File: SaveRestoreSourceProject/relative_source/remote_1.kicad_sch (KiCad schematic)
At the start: 0 parts

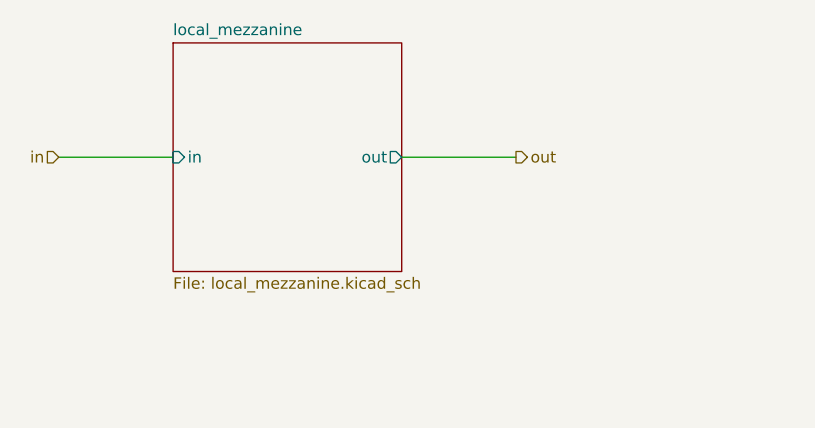
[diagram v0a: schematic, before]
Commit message: Add support for connected drawings, update test template
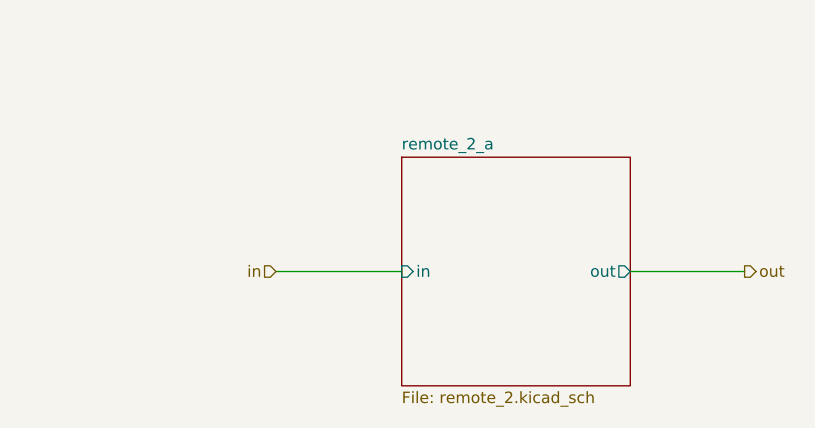
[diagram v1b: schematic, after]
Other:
- removed sheet local_mezzanine
- added sheet remote_2_a (remote_2.kicad_sch)
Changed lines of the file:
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@@
 	(wire
 		(pts
-			(xy 38.1 63.5) (xy 50.8 63.5)
+			(xy 101.6 76.2) (xy 114.3 76.2)
 		)
 		(stroke
@@
 	(wire
 		(pts
-			(xy 76.2 63.5) (xy 88.9 63.5)
+			(xy 62.23 76.2) (xy 76.2 76.2)
 		)
 		(stroke
@@
 		)
 	)
+	(hierarchical_label "out"
+		(shape output)
+		(at 114.3 76.2 0)
+		(fields_autoplaced yes)
+		(effects
+			(font
+				(size 1.27 1.27)
+			)
+			(justify left)
+		)
+	)
 	(hierarchical_label "in"
 		(shape input)
-		(at 38.1 63.5 180)
+		(at 62.23 76.2 180)
 		(fields_autoplaced yes)
 		(effects
@@
 		)
 	)
-	(hierarchical_label "out"
-		(shape output)
-		(at 88.9 63.5 0)
-		(fields_autoplaced yes)
-		(effects
-			(font
-				(size 1.27 1.27)
-			)
-			(justify left)
-		)
-	)
 	(sheet
-		(at 50.8 50.8)
+		(at 76.2 63.5)
 		(size 25.4 25.4)
 		(fields_autoplaced yes)
@@
 			(color 0 0 0 0.0000)
 		)
-		(property "Sheetname" "local_mezzanine"
-			(at 50.8 50.0884 0)
+		(property "Sheetname" "remote_2_a"
+			(at 76.2 62.7884 0)
 			(effects
 				(font
@@
 			)
 		)
-		(property "Sheetfile" "local_mezzanine.kicad_sch"
-			(at 50.8 76.7846 0)
+		(property "Sheetfile" "remote_2.kicad_sch"
+			(at 76.2 89.4846 0)
 			(effects
 				(font
@@
 		)
 		(pin "out" output
-			(at 76.2 63.5 0)
+			(at 101.6 76.2 0)
 			(effects
 				(font
@@
 		)
 		(pin "in" input
-			(at 50.8 63.5 180)
+			(at 76.2 76.2 180)
 			(effects
 				(font
@@
 		(instances
 			(project "save_restore_source_project"
-				(path "/c2758c0b-1161-4b10-8169-92fe64b84f07/9149b517-907e-476c-b9fd-b9a200e02b90"
-					(page "9")
+				(path "/c2758c0b-1161-4b10-8169-92fe64b84f07/247660e6-4fde-4c90-8d89-8b2cc3aad5c3"
+					(page "13")
 				)
 			)
